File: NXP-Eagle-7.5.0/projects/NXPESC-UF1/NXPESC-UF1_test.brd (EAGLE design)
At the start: 66 x 41.6 mm, 2 parts, among them U1 MKV31F512VLL12-M, U2 MC34GD3000EP

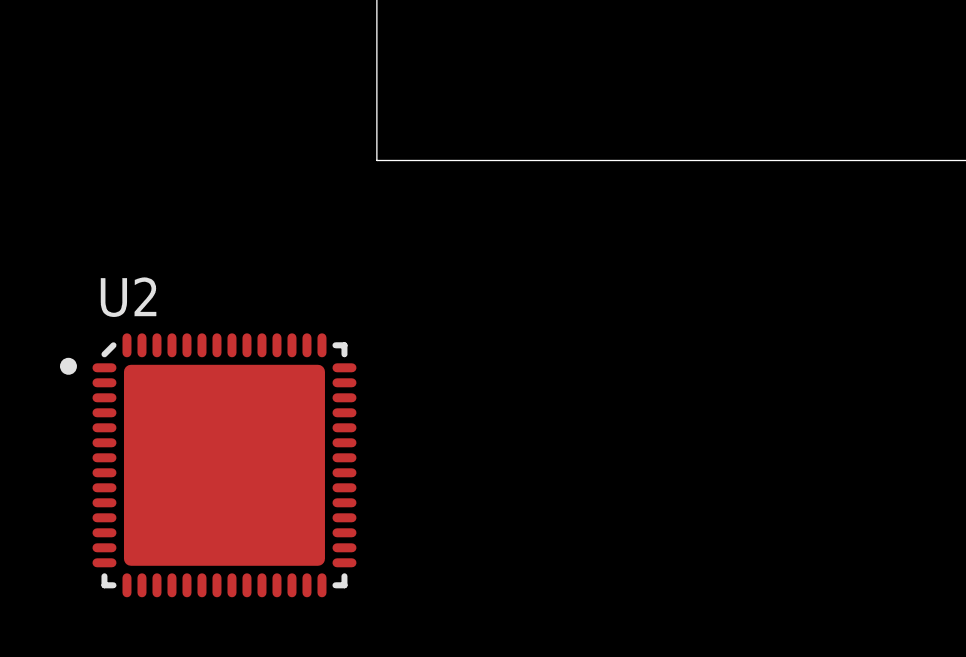
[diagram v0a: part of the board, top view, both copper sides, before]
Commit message: Add FAN78888 device
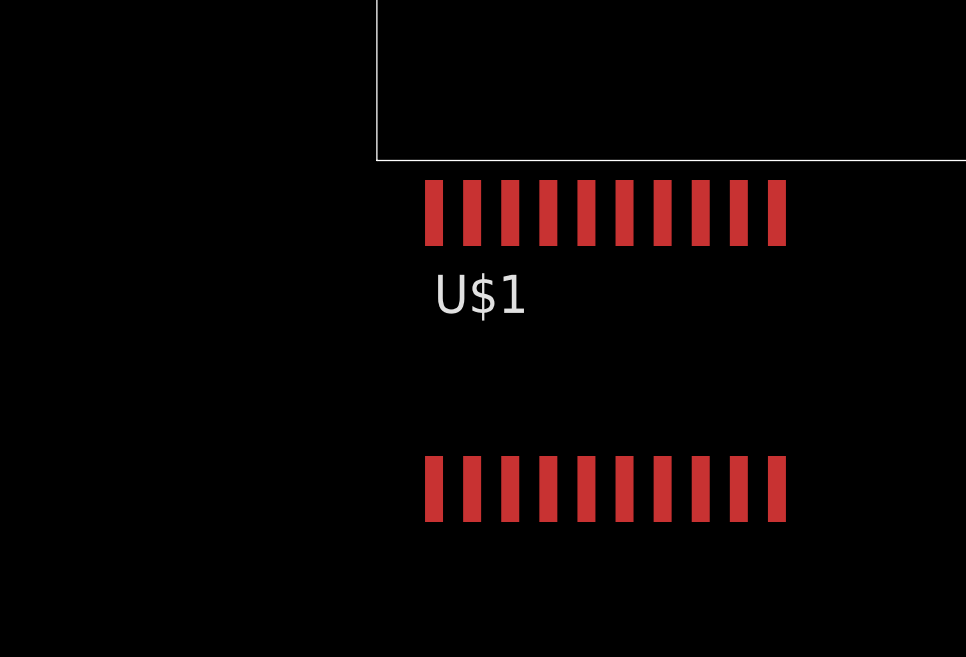
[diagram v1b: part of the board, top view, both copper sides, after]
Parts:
- removed U2: MC34GD3000EP, MC34GD3000EP-None-Symbol-Eagle-1:QFN50P800X800X100-57N
- added U$1: FAN7888, FAN7888:SOIC-20
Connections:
- removed net EP: U2.57
- removed net GND: U2.38, U2.39
- removed net PGND: U2.9
- removed net VPUMP: U2.15
- removed net VPWR: U2.6
- new net VB1: U$1.20
- new net VB2: U$1.16
- new net VB3: U$1.10
- new net VS1: U$1.18
- new net VS2: U$1.14
- new net VS3: U$1.8
- net VDD: now also U$1.12
- net VSS: no longer U2.37
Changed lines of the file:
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@@
 <?xml version="1.0" encoding="utf-8"?>
 <!DOCTYPE eagle SYSTEM "eagle.dtd">
-<eagle version="7.6.0">
+<eagle version="7.3.0">
 <drawing>
 <settings>
@@
 <elements>
 <element name="U1" library="MKV31F512VLL12" package="LQFP-100_14X14X1_7-M" value="MKV31F512VLL12-M" x="40.64" y="24.13"/>
-<element name="U2" library="MC34GD3000EP-None-Symbol-Eagle-1" package="QFN50P800X800X100-57N" value="MC34GD3000EP" x="-5.08" y="-10.16">
-<attribute name="MANUFACTURER" value="NXP" x="-5.08" y="-10.16" size="1.778" layer="27" display="off"/>
-</element>
+<element name="U$1" library="FAN7888" package="SOIC-20" value="FAN7888" x="7.62" y="-6.35"/>
 </elements>
 <signals>
@@
 <signal name="VSS">
 <contactref element="U1" pad="9"/>
-<contactref element="U2" pad="37"/>
-<wire x1="-1.08" y1="-9.41" x2="32.9642" y2="26.13" width="0" layer="19" extent="1-1"/>
 </signal>
 <signal name="VDD">
 <contactref element="U1" pad="8"/>
-</signal>
-<signal name="VPWR">
-<contactref element="U2" pad="6"/>
-</signal>
-<signal name="PGND">
-<contactref element="U2" pad="9"/>
-</signal>
-<signal name="VPUMP">
-<contactref element="U2" pad="15"/>
-</signal>
-<signal name="GND">
-<contactref element="U2" pad="38"/>
-<contactref element="U2" pad="39"/>
-<wire x1="-1.08" y1="-8.41" x2="-1.08" y2="-8.91" width="0" layer="19" extent="1-1"/>
-</signal>
-<signal name="EP">
-<contactref element="U2" pad="57"/>
+<contactref element="U$1" pad="12"/>
+<wire x1="12.065" y1="-1.75" x2="32.9642" y2="26.63" width="0" layer="19" extent="1-1"/>
+</signal>
+<signal name="VB1">
+<contactref element="U$1" pad="20"/>
+</signal>
+<signal name="VB3">
+<contactref element="U$1" pad="10"/>
+</signal>
+<signal name="VS2">
+<contactref element="U$1" pad="14"/>
+</signal>
+<signal name="VS3">
+<contactref element="U$1" pad="8"/>
+</signal>
+<signal name="VS1">
+<contactref element="U$1" pad="18"/>
+</signal>
+<signal name="VB2">
+<contactref element="U$1" pad="16"/>
 </signal>
 </signals>

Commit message: Begin sch
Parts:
- added C1: (no value), pixhawk2:EIA3216
- moved U$1 49.4 mm to (41.9, 29.2)
- moved U1 20.4 mm to (20.3, 22.9)
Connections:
- new net GND: U$1.11
- new net N$5: U$1.1, U1.71
- new net N$6: U$1.2, U1.72
- new net N$7: U$1.3, U1.77
- new net N$8: U$1.4, U1.76
- net VDD: now also C1.A
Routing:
- net VDD: track 0.00 -> 29.7 mm
- net N$7: track 0.00 -> 18.6 mm
- net N$6: track 0.00 -> 11.4 mm

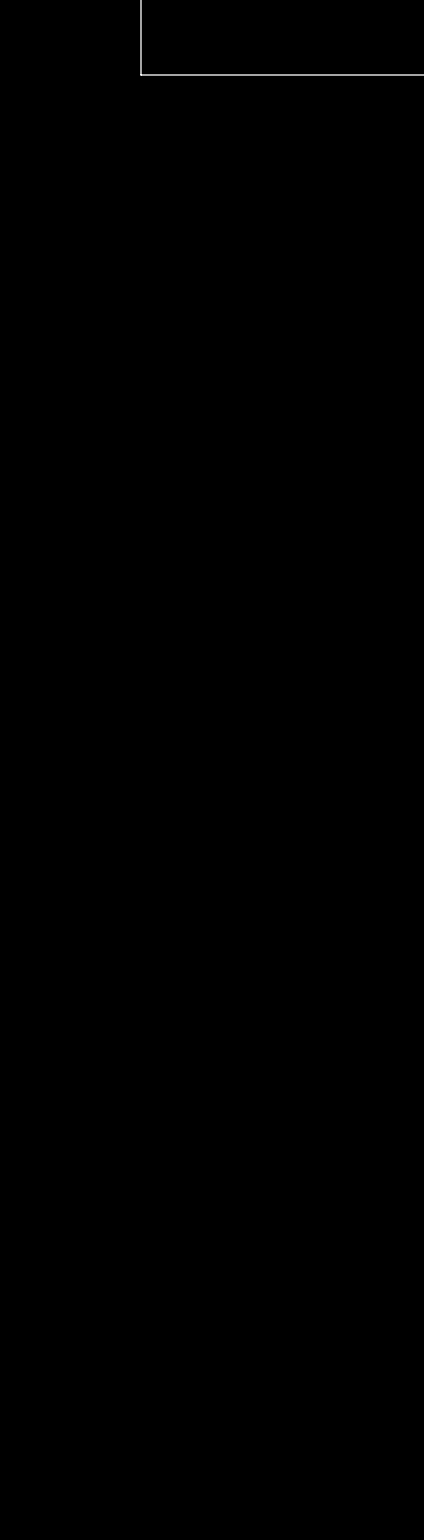
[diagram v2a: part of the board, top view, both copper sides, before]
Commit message: Adding library and datasheet parts
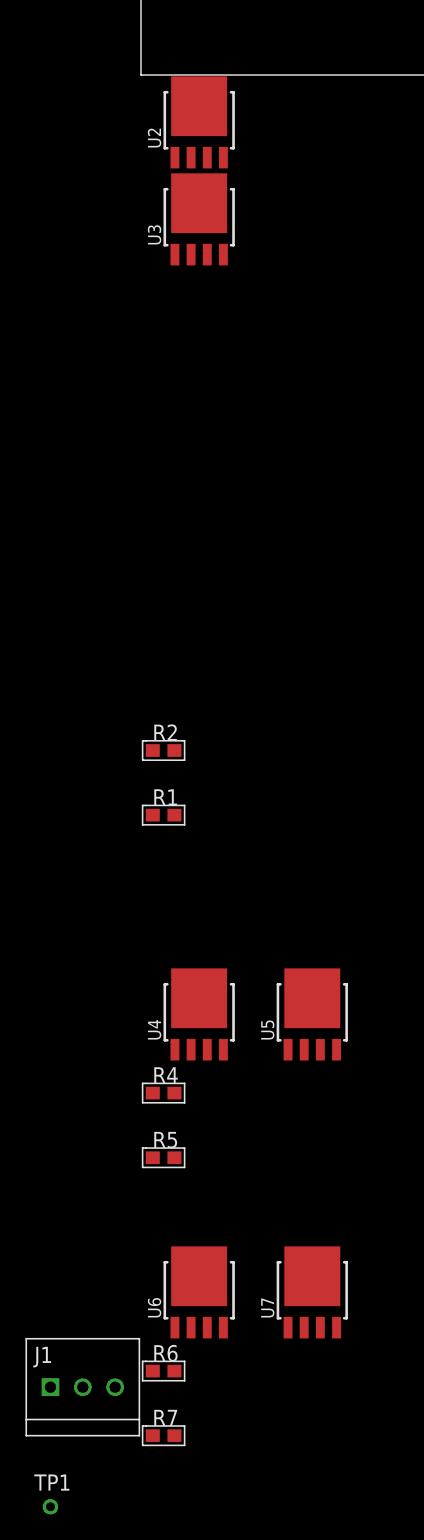
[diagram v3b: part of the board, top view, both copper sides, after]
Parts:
- added J1: FLH1-03SZ-S3A-T, etc-connector-003a:J3
- added R1, R2, R4, R5, R6, R7: RESC0603-200R-1, etc-rcl:C0603
- added TP1: (no value), etc-connector-003a:TP-SMLL
- added U2, U3, U4, U5, U6, U7: PSMN1R4-30YLD, PSMN1R2-25YL_115:LFPAK56
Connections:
- removed net VS1: U$1.18
- removed net VS2: U$1.14
- removed net VS3: U$1.8
- new net HOA: R2.1, U$1.19
- new net HOB: R4.1, U$1.15
- new net HOC: R6.1, U$1.9
- new net LOA: R1.1, U$1.17
- new net LOB: R5.1, U$1.13
- new net LOC: R7.1, U$1.7
- new net N$11: R2.2, U2.4
- new net N$12: R1.2, U3.4
- new net N$13: R4.2, U4.4
- new net N$14: R5.2, U5.4
- new net N$15: R6.2, U6.4
- new net N$16: R7.2, U7.4
- new net N$2: TP1.1, U2.5, U4.5, U6.5
- new net PH_A: J1.1, U$1.18, U2.1, U2.2, U2.3, U3.5
- new net PH_B: J1.2, U$1.14, U4.1, U4.2, U4.3, U5.5
- new net PH_C: J1.3, U$1.8, U6.1, U6.2, U6.3, U7.5
- net GND: now also C1.C
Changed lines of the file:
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@@
 <?xml version="1.0" encoding="utf-8"?>
 <!DOCTYPE eagle SYSTEM "eagle.dtd">
-<eagle version="7.3.0">
+<eagle version="7.6.0">
 <drawing>
 <settings>
@@
 <element name="U$1" library="FAN7888" package="SOIC-20" value="FAN7888" x="41.91" y="29.21"/>
 <element name="C1" library="pixhawk2" package="EIA3216" value="" x="54.61" y="16.51" rot="R90"/>
+<element name="U2" library="PSMN1R2-25YL_115" package="LFPAK56" value="PSMN1R4-30YLD" x="4.572" y="-3.556"/>
+<element name="U3" library="PSMN1R2-25YL_115" package="LFPAK56" value="PSMN1R4-30YLD" x="4.572" y="-11.176"/>
+<element name="R2" library="etc-rcl" package="C0603" value="RESC0603-200R-1" x="1.778" y="-53.086"/>
+<element name="R1" library="etc-rcl" package="C0603" value="RESC0603-200R-1" x="1.778" y="-58.166"/>
+<element name="U4" library="PSMN1R2-25YL_115" package="LFPAK56" value="PSMN1R4-30YLD" x="4.572" y="-73.66"/>
+<element name="U5" library="PSMN1R2-25YL_115" package="LFPAK56" value="PSMN1R4-30YLD" x="13.462" y="-73.66"/>
+<element name="R4" library="etc-rcl" package="C0603" value="RESC0603-200R-1" x="1.778" y="-80.01"/>
+<element name="R5" library="etc-rcl" package="C0603" value="RESC0603-200R-1" x="1.778" y="-85.09"/>
+<element name="U6" library="PSMN1R2-25YL_115" package="LFPAK56" value="PSMN1R4-30YLD" x="4.572" y="-95.504"/>
+<element name="U7" library="PSMN1R2-25YL_115" package="LFPAK56" value="PSMN1R4-30YLD" x="13.462" y="-95.504"/>
+<element name="R6" library="etc-rcl" package="C0603" value="RESC0603-200R-1" x="1.778" y="-101.854"/>
+<element name="R7" library="etc-rcl" package="C0603" value="RESC0603-200R-1" x="1.778" y="-106.934"/>
+<element name="J1" library="etc-connector-003a" package="J3" value="FLH1-03SZ-S3A-T" x="-4.572" y="-103.124"/>
+<element name="TP1" library="etc-connector-003a" package="TP-SMLL" value="" x="-7.112" y="-112.522"/>
 </elements>
 <signals>
@@
 <contactref element="U$1" pad="10"/>
 </signal>
-<signal name="VS2">
-<contactref element="U$1" pad="14"/>
-</signal>
-<signal name="VS3">
-<contactref element="U$1" pad="8"/>
-</signal>
-<signal name="VS1">
-<contactref element="U$1" pad="18"/>
-</signal>
 <signal name="VB2">
 <contactref element="U$1" pad="16"/>
@@
 <signal name="GND">
 <contactref element="U$1" pad="11"/>
+<contactref element="C1" pad="C"/>
+<wire x1="54.61" y1="15.11" x2="47.625" y2="33.81" width="0" layer="19" extent="1-1"/>
 </signal>
 <signal name="N$5">
@@
 <wire x1="26.32" y1="30.5358" x2="40.005" y2="24.61" width="0" layer="19" extent="1-1"/>
 </signal>
+<signal name="HOA">
+<contactref element="U$1" pad="19"/>
+<contactref element="R2" pad="1"/>
+<wire x1="0.928" y1="-53.086" x2="37.465" y2="33.81" width="0" layer="19" extent="1-1"/>
+</signal>
+<signal name="LOA">
+<contactref element="U$1" pad="17"/>
+<contactref element="R1" pad="1"/>
+<wire x1="0.928" y1="-58.166" x2="40.005" y2="33.81" width="0" layer="19" extent="1-1"/>
+</signal>
+<signal name="HOB">
+<contactref element="U$1" pad="15"/>
+<contactref element="R4" pad="1"/>
+<wire x1="42.545" y1="33.81" x2="0.928" y2="-80.01" width="0" layer="19" extent="1-1"/>
+</signal>
+<signal name="LOB">
+<contactref element="U$1" pad="13"/>
+<contactref element="R5" pad="1"/>
+<wire x1="45.085" y1="33.81" x2="0.928" y2="-85.09" width="0" layer="19" extent="1-1"/>
+</signal>
+<signal name="HOC">
+<contactref element="U$1" pad="9"/>
+<contactref element="R6" pad="1"/>
+<wire x1="46.355" y1="24.61" x2="0.928" y2="-101.854" width="0" layer="19" extent="1-1"/>
+</signal>
+<signal name="LOC">
+<contactref element="U$1" pad="7"/>
+<contactref element="R7" pad="1"/>
+<wire x1="43.815" y1="24.61" x2="0.928" y2="-106.934" width="0" layer="19" extent="1-1"/>
+</signal>
+<signal name="N$11">
+<contactref element="R2" pad="2"/>
+<contactref element="U2" pad="4"/>
+<wire x1="6.477" y1="-6.496" x2="2.628" y2="-53.086" width="0" layer="19" extent="1-1"/>
+</signal>
+<signal name="N$12">
+<contactref element="R1" pad="2"/>
+<contactref element="U3" pad="4"/>
+<wire x1="6.477" y1="-14.116" x2="2.628" y2="-58.166" width="0" layer="19" extent="1-1"/>
+</signal>
+<signal name="N$13">
+<contactref element="R4" pad="2"/>
+<contactref element="U4" pad="4"/>
+<wire x1="6.477" y1="-76.6" x2="2.628" y2="-80.01" width="0" layer="19" extent="1-1"/>
+</signal>
+<signal name="N$14">
+<contactref element="R5" pad="2"/>
+<contactref element="U5" pad="4"/>
+<wire x1="15.367" y1="-76.6" x2="2.628" y2="-85.09" width="0" layer="19" extent="1-1"/>
+</signal>
+<signal name="N$15">
+<contactref element="R6" pad="2"/>
+<contactref element="U6" pad="4"/>
+<wire x1="6.477" y1="-98.444" x2="2.628" y2="-101.854" width="0" layer="19" extent="1-1"/>
+</signal>
+<signal name="N$16">
+<contactref element="R7" pad="2"/>
+<contactref element="U7" pad="4"/>
+<wire x1="15.367" y1="-98.444" x2="2.628" y2="-106.934" width="0" layer="19" extent="1-1"/>
+</signal>
+<signal name="PH_A">
+<contactref element="U$1" pad="18"/>
+<contactref element="U2" pad="2"/>
+<contactref element="U2" pad="1"/>
+<contactref element="U2" pad="3"/>
+<contactref element="U3" pad="5"/>
+<contactref element="J1" pad="1"/>
+<wire x1="4.572" y1="-10.076" x2="-7.112" y2="-103.124" width="0" layer="19" extent="1-1"/>
+<wire x1="3.937" y1="-6.496" x2="4.572" y2="-10.076" width="0" layer="19" extent="1-1"/>
+<wire x1="2.667" y1="-6.496" x2="3.937" y2="-6.496" width="0" layer="19" extent="1-1"/>
+<wire x1="5.207" y1="-6.496" x2="3.937" y2="-6.496" width="0" layer="19" extent="1-1"/>
+<wire x1="38.735" y1="33.81" x2="5.207" y2="-6.496" width="0" layer="19" extent="1-1"/>
+</signal>
+<signal name="PH_B">
+<contactref element="U$1" pad="14"/>
+<contactref element="U4" pad="2"/>
+<contactref element="U4" pad="1"/>
+<contactref element="U4" pad="3"/>
+<contactref element="U5" pad="5"/>
+<contactref element="J1" pad="2"/>
+<wire x1="2.667" y1="-76.6" x2="-4.572" y2="-103.124" width="0" layer="19" extent="1-1"/>
+<wire x1="3.937" y1="-76.6" x2="2.667" y2="-76.6" width="0" layer="19" extent="1-1"/>
+<wire x1="5.207" y1="-76.6" x2="3.937" y2="-76.6" width="0" layer="19" extent="1-1"/>
+<wire x1="13.462" y1="-72.56" x2="5.207" y2="-76.6" width="0" layer="19" extent="1-1"/>
+<wire x1="43.815" y1="33.81" x2="13.462" y2="-72.56" width="0" layer="19" extent="1-1"/>
+</signal>
+<signal name="PH_C">
+<contactref element="U$1" pad="8"/>
+<contactref element="U6" pad="2"/>
+<contactref element="U6" pad="1"/>
+<contactref element="U6" pad="3"/>
+<contactref element="U7" pad="5"/>
+<contactref element="J1" pad="3"/>
+<wire x1="2.667" y1="-98.444" x2="-2.032" y2="-103.124" width="0" layer="19" extent="1-1"/>
+<wire x1="3.937" y1="-98.444" x2="2.667" y2="-98.444" width="0" layer="19" extent="1-1"/>
+<wire x1="5.207" y1="-98.444" x2="3.937" y2="-98.444" width="0" layer="19" extent="1-1"/>
+<wire x1="13.462" y1="-94.404" x2="5.207" y2="-98.444" width="0" layer="19" extent="1-1"/>
+<wire x1="45.085" y1="24.61" x2="13.462" y2="-94.404" width="0" layer="19" extent="1-1"/>
+</signal>
+<signal name="N$2">
+<contactref element="U2" pad="5"/>
+<contactref element="U6" pad="5"/>
+<contactref element="U4" pad="5"/>
+<contactref element="TP1" pad="1"/>
+<wire x1="4.572" y1="-94.404" x2="-7.112" y2="-112.522" width="0" layer="19" extent="1-1"/>
+<wire x1="4.572" y1="-72.56" x2="4.572" y2="-94.404" width="0" layer="19" extent="1-1"/>
+<wire x1="4.572" y1="-2.456" x2="4.572" y2="-72.56" width="0" layer="19" extent="1-1"/>
+</signal>
 </signals>
